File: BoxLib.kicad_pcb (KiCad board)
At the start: 2 copper layers, 10 parts, among them J1 Generic_2Pos_terminal_block, J2 Solder-Jumper-NO, J3 Solder-Jumper-NO, J4 Solder-Jumper-NO, J5 Solder-Jumper-NC, J6 Solder-Jumper-NC, J7 Solder-Jumper-NC, J8 Solder-Jumper-NO, J9 Solder-Jumper-NC

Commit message: Added LittelFuse 154 series
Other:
- board outline added: 66 x 27.9 mm
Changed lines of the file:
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@@
       (net 5 "unconnected-(J1-Pad2)") (pintype "input"))
   )
+  (gr_line (start 50.8 91.44) (end 50.8 63.5) (layer "Edge.Cuts") (width 0.1))
+  (gr_line (start 116.84 63.5) (end 116.84 91.44) (layer "Edge.Cuts") (width 0.1))
+  (gr_line (start 50.8 63.5) (end 116.84 63.5) (layer "Edge.Cuts") (width 0.1))
+  (gr_line (start 116.84 91.44) (end 50.8 91.44) (layer "Edge.Cuts") (width 0.1))
   (gr_text "${RevNumber}" (at 98.2 64.9) (layer "F.Mask")
     (effects (font (size 1.5 1.5) (thickness 0.3)))

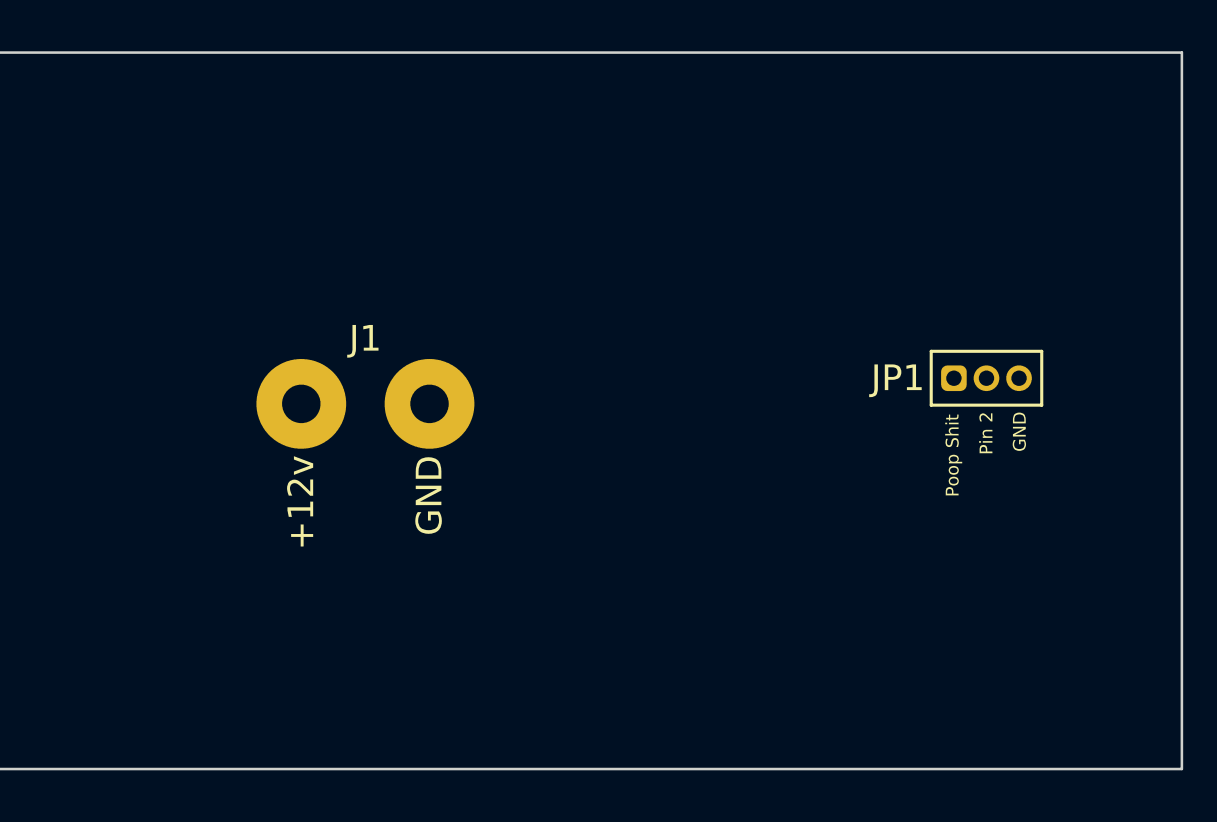
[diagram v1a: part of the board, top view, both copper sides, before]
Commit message: Updated some fuses
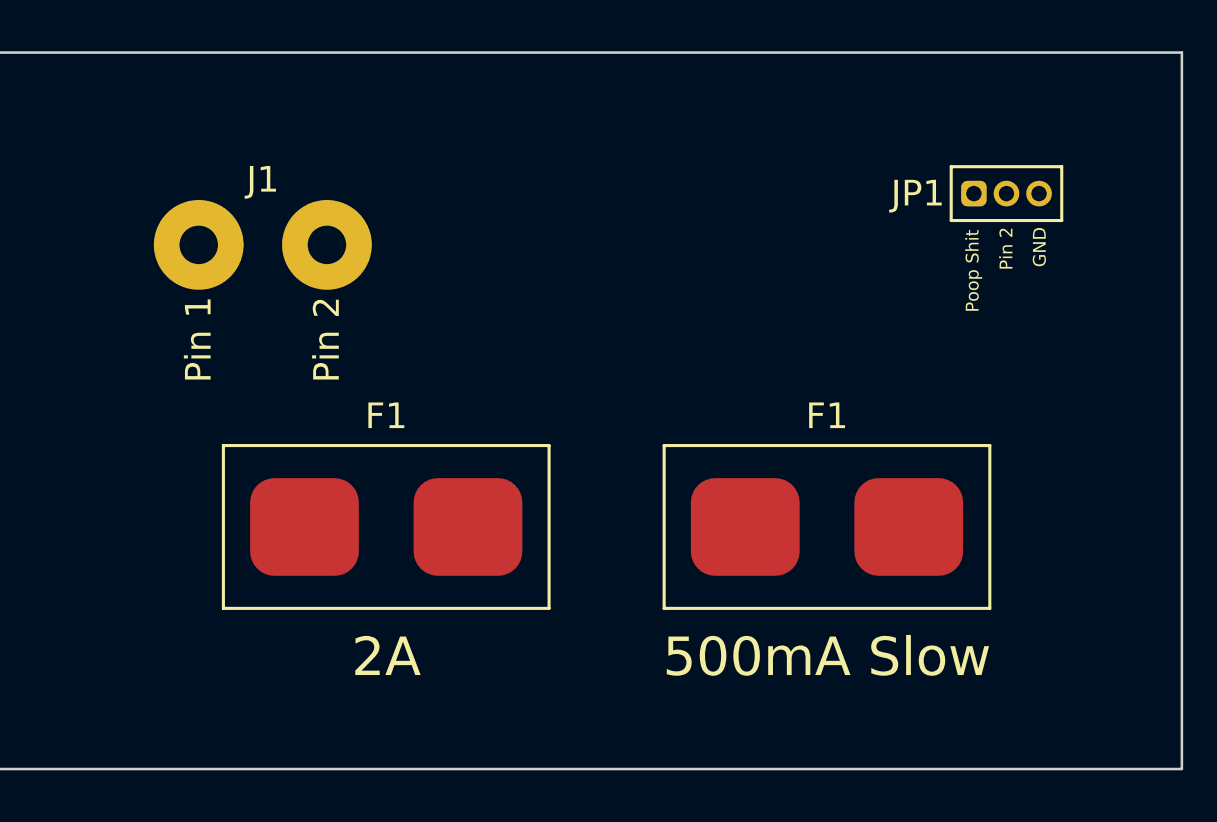
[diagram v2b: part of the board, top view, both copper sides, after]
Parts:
- added F1: Littelfuse_154_0.5A_Slow, BoxLib:Fuse-Current-Littelfuse-Nano2_154, F.Cu at (103.0, 82.0)
- added F1: Littelfuse_154_2A, BoxLib:Fuse-Current-Littelfuse-Nano2_154, F.Cu at (85.8, 82.0)
- moved J1 7.38 mm to (81.0, 71.0)
- moved JP1 7.24 mm to (110.0, 69.0)

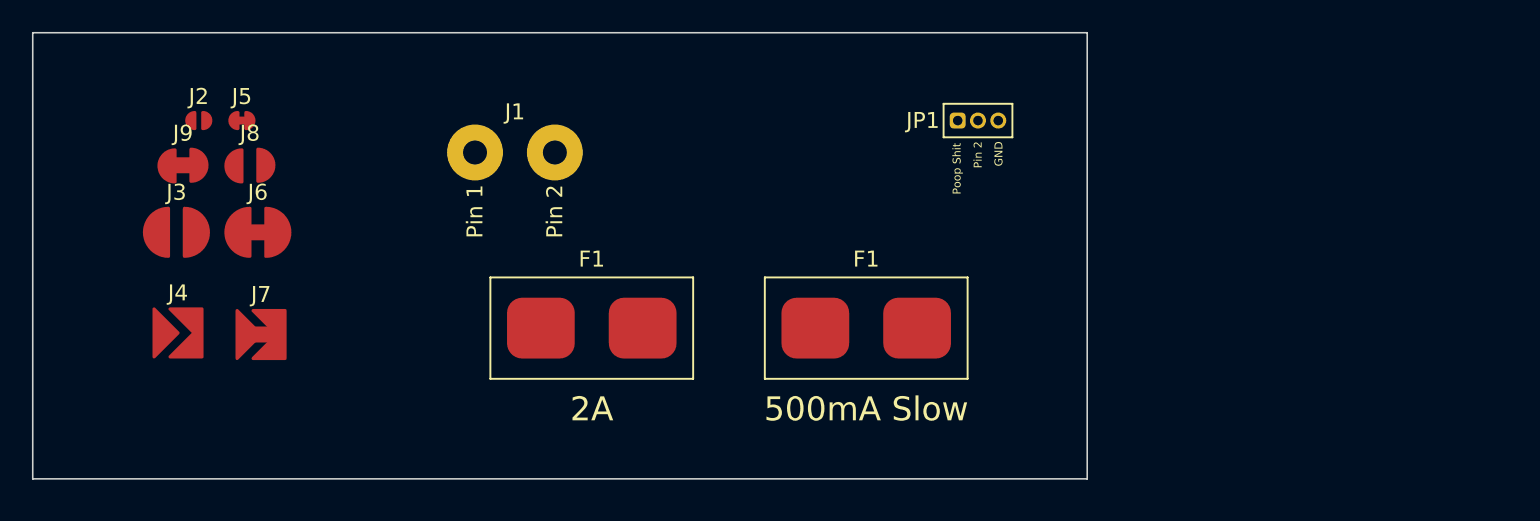
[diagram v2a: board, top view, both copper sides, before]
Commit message: Added a couple of Adafruit QT Pys
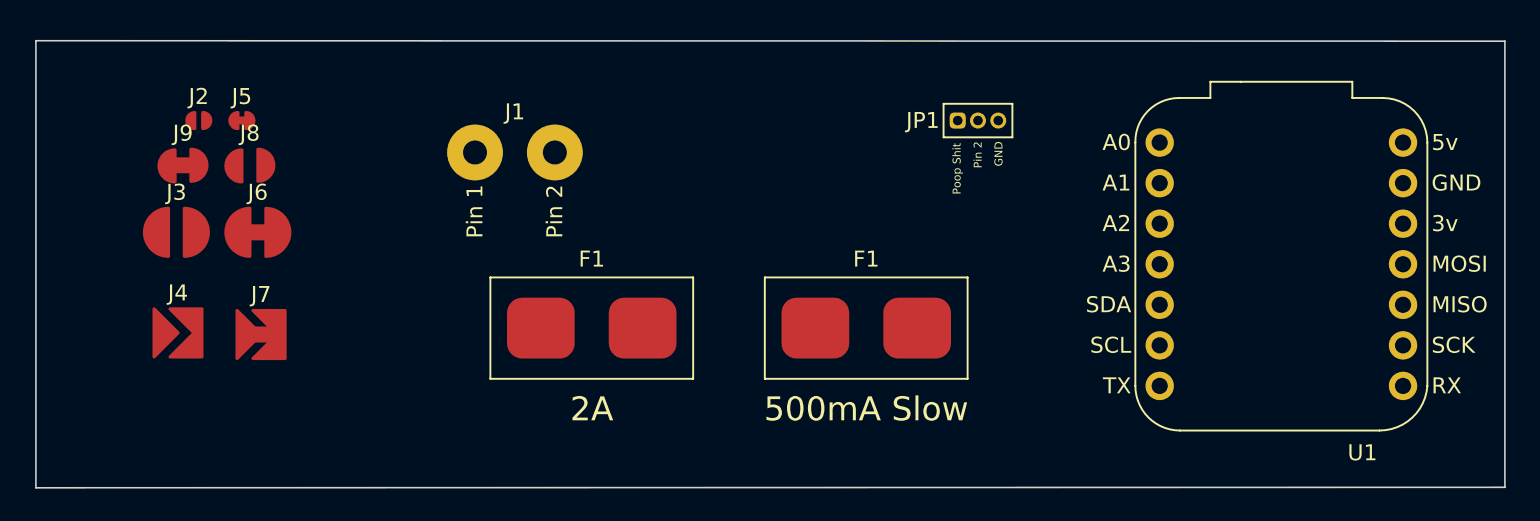
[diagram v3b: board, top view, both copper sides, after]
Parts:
- added U1: QT_Py_RP2040, BoxLib:Adafruit-QT_Py_RP2040-PTH, F.Cu at (129.0, 78.0)
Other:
- board size 66 x 27.9 mm -> 92 x 28 mm

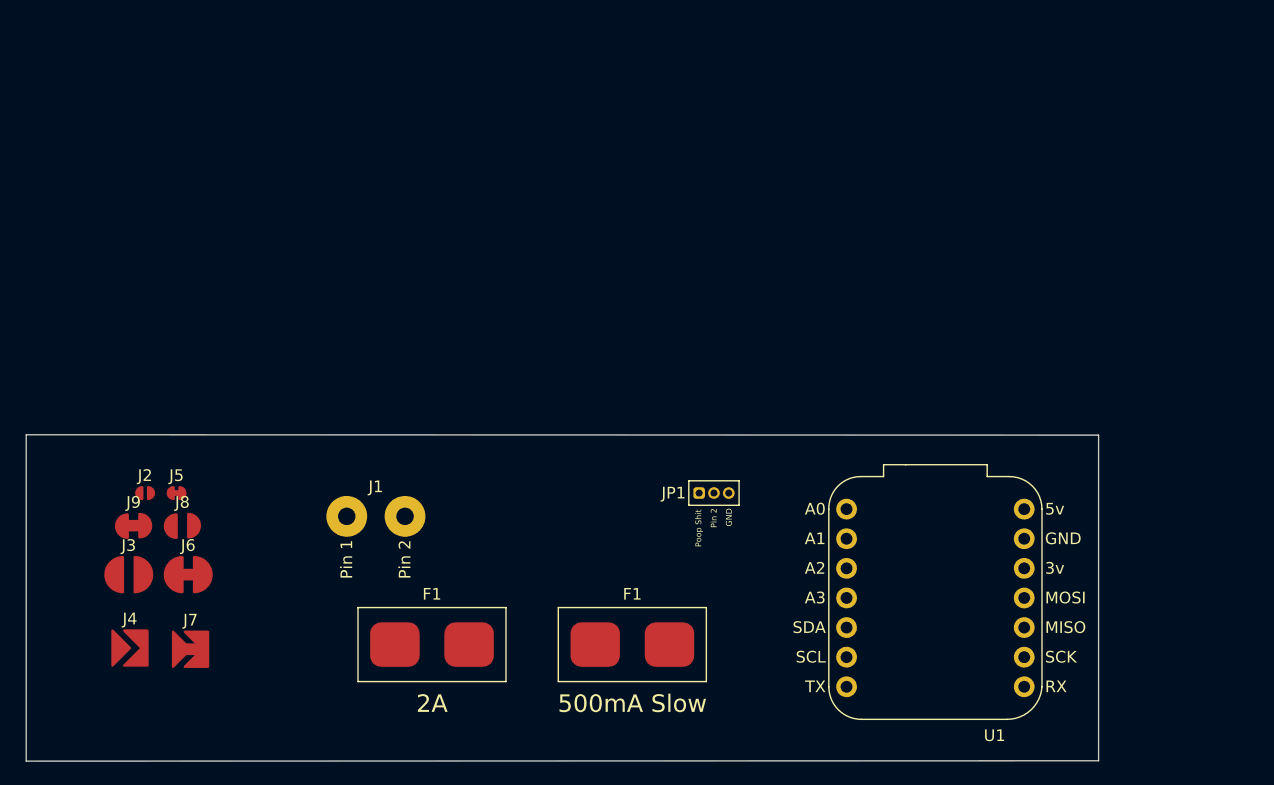
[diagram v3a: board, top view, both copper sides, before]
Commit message: Updats to linking, NEW LED
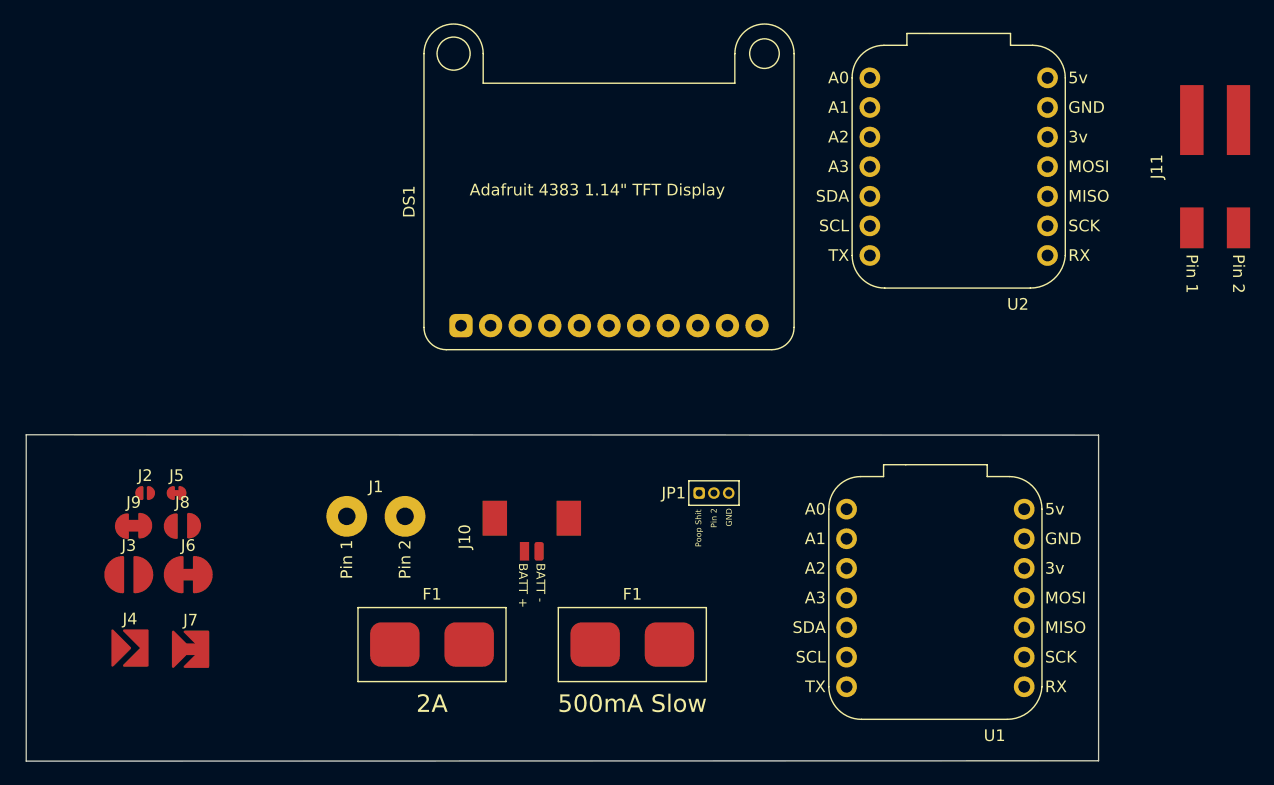
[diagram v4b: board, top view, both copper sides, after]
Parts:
- added DS1: Adafruit-4383, BoxLib:Adafruit-1_14-tft-display-4383, F.Cu at (101.0, 44.0)
- added J10: Molex_2Pos_terminal_block_1.25mm-0532614002, BoxLib:Connector-SMD-2Pos-Molex-0532614002, F.Cu at (94.4, 72.8)
- added J11: Generic_2Pos_terminal_block, BoxLib:Connector-SMD-2Pos-Wago-2060-452_998-404, F.Cu at (153.0, 41.0)
- added U2: QT_Py, BoxLib:Adafruit-QT_Py-PTH, F.Cu at (131.0, 41.0)

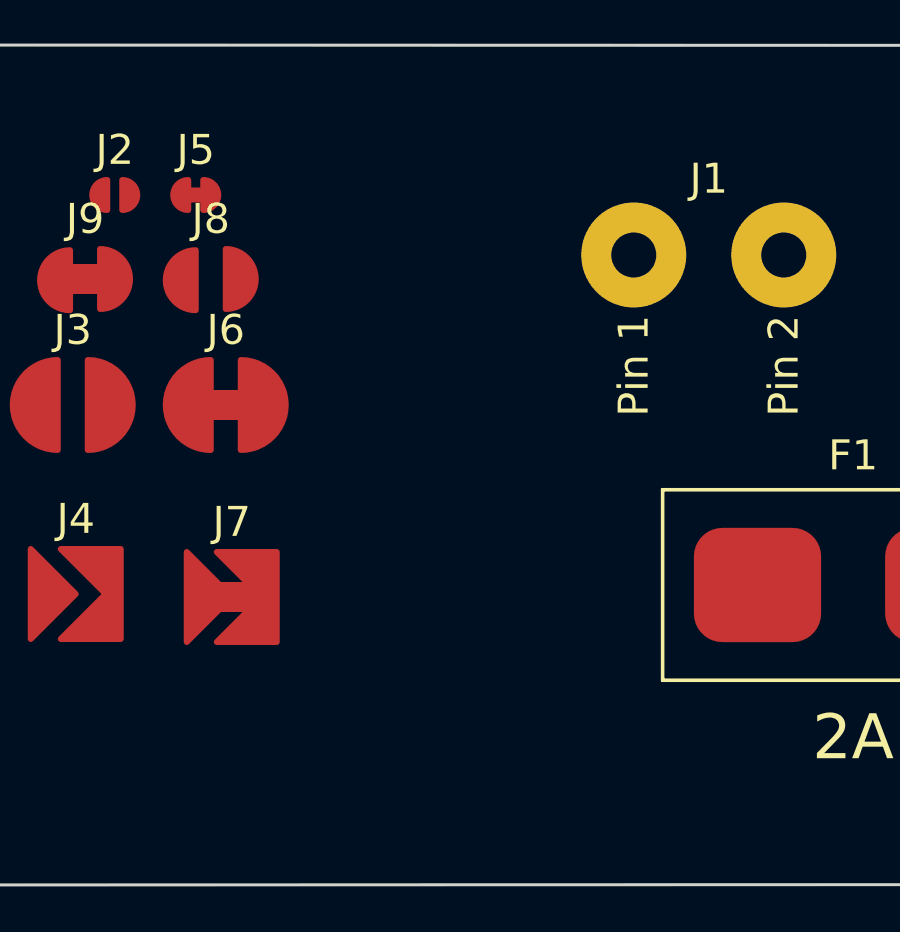
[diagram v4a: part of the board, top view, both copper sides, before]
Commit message: Added PTH varients of devices
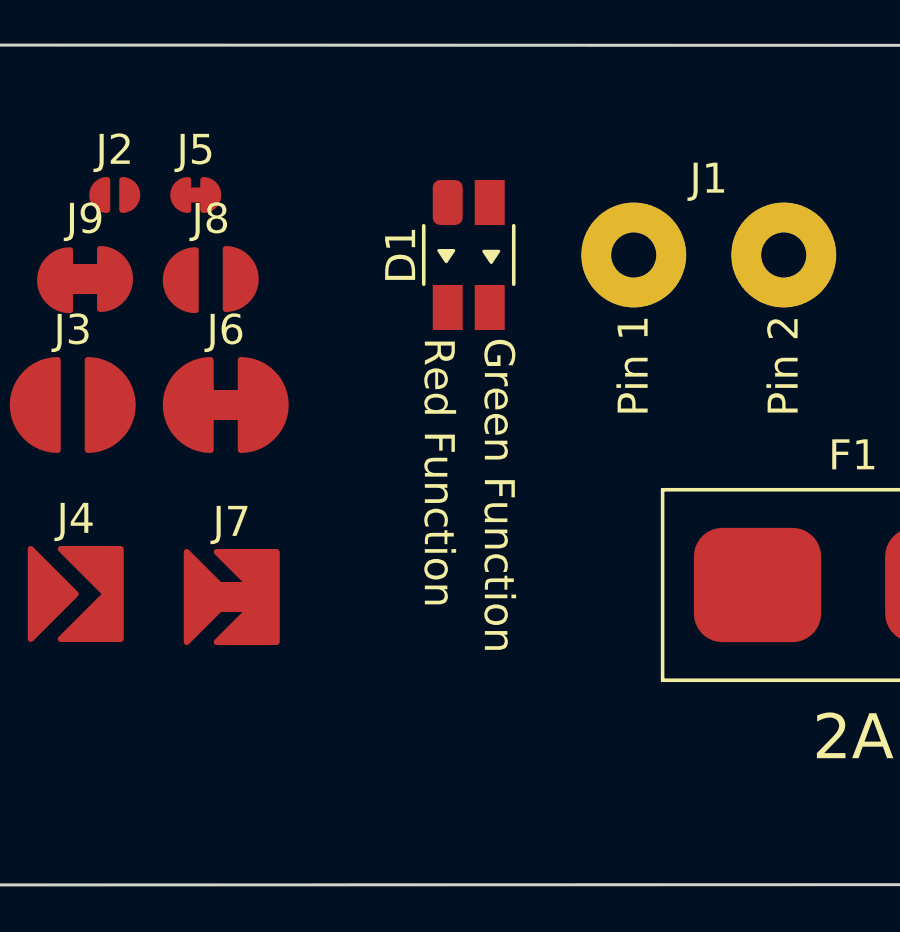
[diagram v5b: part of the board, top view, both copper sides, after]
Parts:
- added D1: LED-LTST-C155GEKT, BoxLib:LED-LTST-C155GEKT, F.Cu at (73.0, 71.0)
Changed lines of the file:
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@@
   (net 55 "unconnected-(U2-PadSDA)")
   (net 56 "unconnected-(U2-PadTX)")
+  (net 57 "unconnected-(D1-Pad1)")
+  (net 58 "unconnected-(D1-Pad2)")
+  (net 59 "unconnected-(D1-Pad3)")
+  (net 60 "unconnected-(D1-Pad4)")
+  (footprint "BoxLib:LED-LTST-C155GEKT" (layer "F.Cu")
+    (at 73 71)
+    (property "Green" "Green Function")
+    (property "MPN" "C155GEKT")
+    (property "Manufacturer" "LTST")
+    (property "Red" "Red Function")
+    (property "Sheetfile" "BoxLib.kicad_sch")
+    (property "Sheetname" "")
+    (attr smd)
+    (fp_text reference "D1" (at -2.25 0 90 unlocked) (layer "F.SilkS")
+      (effects (font (size 1 1) (thickness 0.15)))
+    )
+    (fp_text value "LED-LTST-C155GEKT" (at 0 -3.75 unlocked) (layer "F.Fab")
+      (effects (font (size 1 1) (thickness 0.15)))
+    )
+    (fp_text user "${Red}" (at -1 2.75 270 unlocked) (layer "F.SilkS")
+      (effects (font (size 1 1) (thickness 0.15)) (justify left))
+    )
+    (fp_text user "${Green}" (at 1 2.75 270 unlocked) (layer "F.SilkS")
+      (effects (font (size 1 1) (thickness 0.15)) (justify left))
+    )
+    (fp_text user "${REFERENCE}" (at 0.25 0 90 unlocked) (layer "F.Fab")
+      (effects (font (size 1 1) (thickness 0.15)))
+    )
+    (fp_line (start -1.5 -0.975) (end -1.5 0.975) (layer "F.SilkS") (width 0.12))
+    (fp_line (start 1.5 -0.975) (end 1.5 0.975) (layer "F.SilkS") (width 0.12))
+    (fp_poly (pts
+        (xy 1 -0.125)
+        (xy 0.75 0.25)
+        (xy 0.5 -0.125)
+      ) (layer "F.SilkS") (width 0.1) (fill solid))
+    (fp_poly (pts
+        (xy -0.5 -0.15)
+        (xy -0.75 0.225)
+        (xy -1 -0.15)
+      ) (layer "F.SilkS") (width 0.1) (fill solid))
+    (fp_rect (start -1.5 -2.75) (end 1.5 2.75) (layer "F.CrtYd") (width 0.05) (fill none))
+    (pad "1" smd roundrect (at -0.7 -1.75) (size 1 1.5) (layers "F.Cu" "F.Paste" "F.Mask") (roundrect_rratio 0.25)
+      (net 57 "unconnected-(D1-Pad1)") (pintype "passive"))
+    (pad "2" smd rect (at 0.7 -1.75) (size 1 1.5) (layers "F.Cu" "F.Paste" "F.Mask")
+      (net 58 "unconnected-(D1-Pad2)") (pintype "passive"))
+    (pad "3" smd rect (at -0.7 1.75) (size 1 1.5) (layers "F.Cu" "F.Paste" "F.Mask")
+      (net 59 "unconnected-(D1-Pad3)") (pintype "passive"))
+    (pad "4" smd rect (at 0.7 1.75) (size 1 1.5) (layers "F.Cu" "F.Paste" "F.Mask")
+      (net 60 "unconnected-(D1-Pad4)") (pintype "passive"))
+    (model "${BOXLIB}/3D Models/LTST-C155GEKT.STEP"
+      (offset (xyz 0 0 0))
+      (scale (xyz 1 1 1))
+      (rotate (xyz -90 0 0))
+    )
+  )
   (footprint "BoxLib:Jumper-Solder-Chevron-3mm-NC" (layer "F.Cu")
     (at 65.1 82.4)
